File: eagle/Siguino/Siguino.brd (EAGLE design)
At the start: 70.5 x 38.7 mm, 35 parts, among them J1 FTDI Basic, Q1 MOSFET P-CH 20V 5.3A SOT-23, U1 ATMEGA328P_TQFP, U2 LIS3MDLTR_LIS3MDLTR, U3 SPARKFUN-SENSORS_LIS3DH, U4 BME280, Y1 8MHz

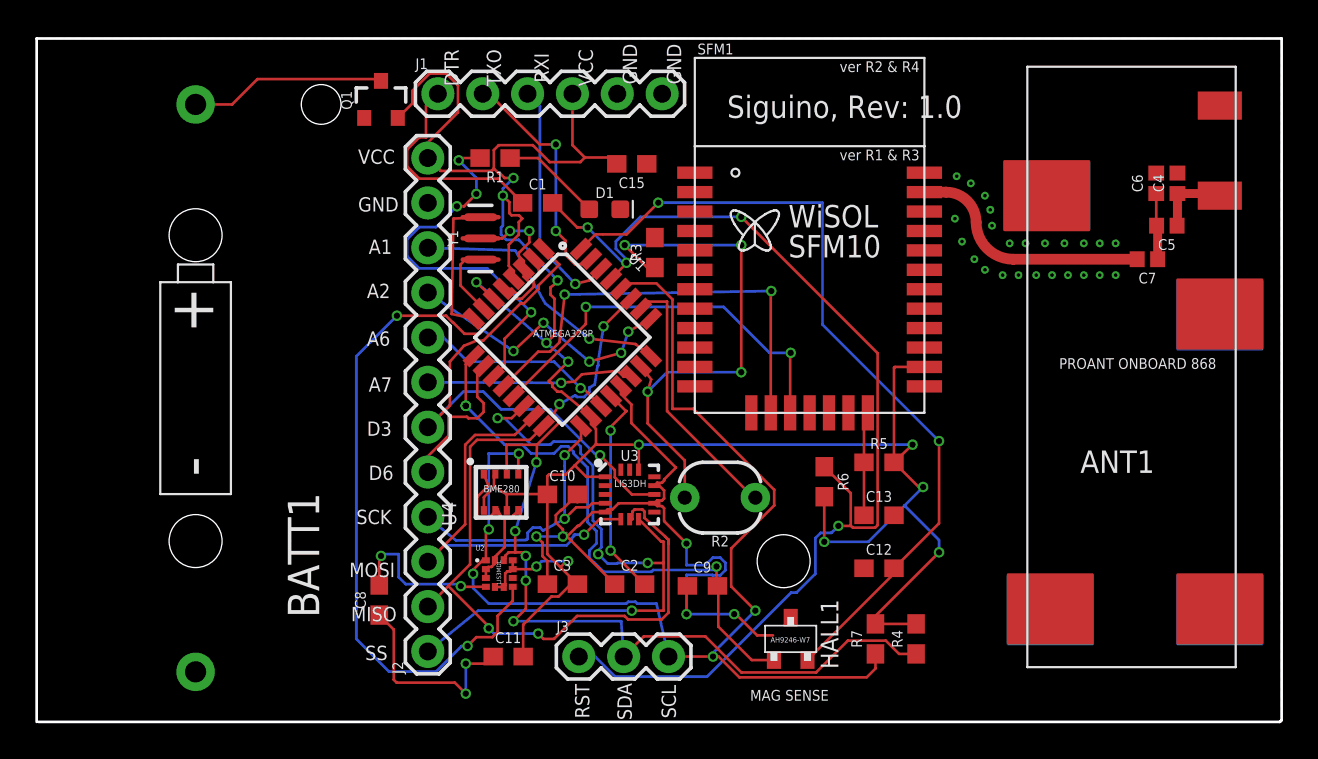
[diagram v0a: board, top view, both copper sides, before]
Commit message: Fixed issue with hatching on antenna pads causing RF issues
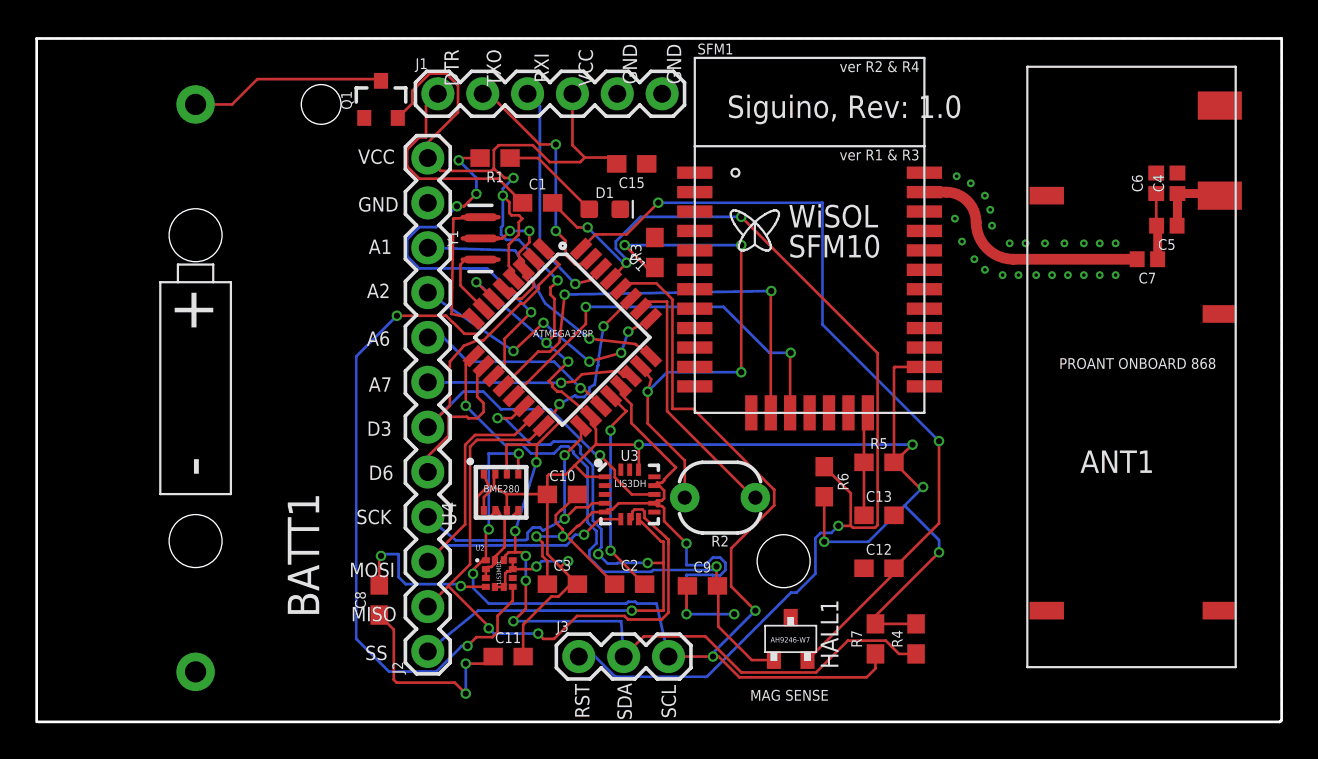
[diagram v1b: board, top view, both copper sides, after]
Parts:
- ANT1: device Siguino:PROANT_ONBOARD_SMD_2400 -> proant:ONBOARD_SMD_2400
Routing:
- net GND: track 76.5 -> 73.0 mm
- net HALL_POWER: vias 3 -> 2
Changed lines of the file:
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@@
 <attribute name="VALUE" x="48.1" y="14.338" size="0.6096" layer="27" font="vector" ratio="20" align="top-center"/>
 </element>
-<element name="ANT1" library="Siguino" package="PROANT_ONBOARD_SMD_2400" value="PROOB471" x="62.4" y="20.5" smashed="yes">
+<element name="ANT1" library="proant" package="ONBOARD_SMD_2400" value="PROOB471" x="62.4" y="20.5" smashed="yes">
 <attribute name="NAME" x="59.5" y="14.5" size="1.27" layer="25"/>
 <attribute name="VALUE" x="59.5" y="18.3" size="1.27" layer="27"/>
@@
 <contactref element="C12" pad="1"/>
 <contactref element="C13" pad="2"/>
-<contactref element="ANT1" pad="GND"/>
 <wire x1="25.54" y1="27.78" x2="26.78" y2="27.78" width="0.1524" layer="1"/>
 <wire x1="26.78" y1="27.78" x2="27.2" y2="28.2" width="0.1524" layer="1"/>
@@
 <wire x1="37.2" y1="6.5" x2="39.9" y2="6.5" width="0.1524" layer="16"/>
 <via x="39.9" y="6.5" extent="1-16" drill="0.35"/>
-<wire x1="39.9" y1="6.5" x2="40" y2="6.5" width="0.1524" layer="1"/>
-<wire x1="40" y1="6.5" x2="41.2" y2="5.3" width="0.1524" layer="1"/>
-<wire x1="41.2" y1="5.3" x2="42.1" y2="5.3" width="0.1524" layer="1"/>
 <contactref element="C15" pad="1"/>
 <contactref element="C6" pad="2"/>
@@
 <wire x1="36.6" y1="14.8" x2="35.9312" y2="14.1312" width="0.1524" layer="1"/>
 <wire x1="35.9312" y1="14.1312" x2="35.9312" y2="14.0566625" width="0.1524" layer="1"/>
-<wire x1="30.3988" y1="11.0988" x2="30.2" y2="10.9" width="0.1524" layer="1"/>
-<wire x1="31.02" y1="12.82880625" x2="31.02" y2="13.28" width="0.1524" layer="1"/>
 <wire x1="35.8133375" y1="12.9388" x2="35.9312" y2="13.0566625" width="0.1524" layer="1"/>
 <wire x1="35.9312" y1="13.0566625" x2="35.9312" y2="13.5033375" width="0.1524" layer="1"/>
@@
 <wire x1="26.35" y1="9.56" x2="26.35" y2="9.3754625" width="0.15" layer="1"/>
 <wire x1="26.35" y1="9.3754625" x2="26.2662" y2="9.2916625" width="0.15" layer="1"/>
+<contactref element="ANT1" pad="GND"/>
 </signal>
 <signal name="VCC">
@@
 <contactref element="U4" pad="P$8"/>
 <contactref element="U4" pad="P$2"/>
-<wire x1="27" y1="12.35" x2="27.025" y2="12.375" width="0.1524" layer="1"/>
 <wire x1="25.725" y1="12.375" x2="25.725" y2="13.125" width="0.1524" layer="1"/>
 <wire x1="25.725" y1="13.125" x2="26.3" y2="13.7" width="0.1524" layer="1"/>
@@
 <wire x1="30.9" y1="25.2" x2="31.70294375" y2="25.4" width="0.1524" layer="1"/>
 <wire x1="31.70294375" y1="25.4" x2="32.356796875" y2="26.053853125" width="0.1524" layer="1"/>
-<wire x1="28.8012" y1="27.3988" x2="28.9" y2="27.3" width="0.1524" layer="16"/>
 <wire x1="28.9" y1="27.3" x2="28.9" y2="35.27" width="0.1524" layer="16"/>
 <wire x1="28.9" y1="35.27" x2="28.2" y2="35.97" width="0.1524" layer="16"/>
@@
 <contactref element="J2" pad="6"/>
 <wire x1="25.31153125" y1="21.98975" x2="25.68975" y2="21.98975" width="0.1524" layer="1"/>
-<wire x1="30" y1="26.3" x2="29.999796875" y2="26.3" width="0.1524" layer="1"/>
 <wire x1="25.31153125" y1="21.98975" x2="24.6" y2="21.7" width="0.1524" layer="1"/>
 <wire x1="24.6" y1="21.7" x2="23.8" y2="20.8" width="0.1524" layer="1"/>
@@
 <wire x1="27.982125" y1="24.08558125" x2="28.820109375" y2="24.923565625" width="0.1524" layer="1"/>
 <wire x1="28.820109375" y1="24.923565625" x2="28.820109375" y2="25.120109375" width="0.1524" layer="1"/>
-<wire x1="28.820109375" y1="25.120109375" x2="30" y2="26.3" width="0.1524" layer="1"/>
+<wire x1="30" y1="26.3" x2="28.820109375" y2="25.120109375" width="0.1524" layer="1"/>
 <contactref element="U3" pad="11"/>
 <wire x1="33.1388" y1="14.2466625" x2="33.1388" y2="14.6612" width="0.1524" layer="1"/>
@@
 <wire x1="24.56" y1="19.1" x2="22.55" y2="17.09" width="0.1524" layer="16"/>
 <contactref element="U1" pad="1"/>
-<wire x1="29.114571875" y1="27.185225" x2="29.114775" y2="27.185225" width="0.15" layer="1"/>
-<wire x1="29.114775" y1="27.185225" x2="30" y2="26.3" width="0.15" layer="1"/>
+<wire x1="29.114571875" y1="27.185225" x2="29.114775" y2="27.185225" width="0.1524" layer="1"/>
+<wire x1="29.114775" y1="27.185225" x2="30" y2="26.3" width="0.1524" layer="1"/>
 </signal>
 <signal name="D6">
@@
 <contactref element="U1" pad="25"/>
 <contactref element="J2" pad="9"/>
-<wire x1="22.56" y1="24.7" x2="22.55" y2="24.71" width="0.1524" layer="16"/>
 <wire x1="22.55" y1="24.71" x2="27.4" y2="21.4" width="0.1524" layer="16"/>
 <via x="27.4" y="21.4" extent="1-16" drill="0.35"/>
@@
 <via x="31.4" y="11" extent="1-16" drill="0.35"/>
 <wire x1="31.4" y1="11" x2="30.9" y2="11" width="0.1524" layer="16"/>
-<wire x1="30.9" y1="11" x2="30.80880625" y2="11" width="0.1524" layer="16"/>
 <wire x1="23.4788" y1="10.3988" x2="22.55" y2="9.47" width="0.1524" layer="16"/>
 <wire x1="30.7012" y1="10.69239375" x2="30.40760625" y2="10.3988" width="0.1524" layer="16"/>
@@
 <signal name="N$4">
 <contactref element="C5" pad="1"/>
-<contactref element="ANT1" pad="RF_FEED"/>
-<wire x1="67.12" y1="29.92" x2="67.4" y2="30.2" width="0.1524" layer="1"/>
-<wire x1="67.22" y1="30.02" x2="67.4" y2="30.2" width="0.1524" layer="1"/>
 <contactref element="C4" pad="1"/>
-<wire x1="66.72" y1="30.32" x2="67.12" y2="29.92" width="0.1524" layer="1"/>
+<wire x1="67.12" y1="29.92" x2="66.72" y2="30.32" width="0.1524" layer="1"/>
 <wire x1="64.98" y1="28.5" x2="65" y2="28.52" width="0.508" layer="1"/>
 <wire x1="65" y1="28.52" x2="65" y2="30.32" width="0.508" layer="1"/>
 <wire x1="65" y1="30.32" x2="66.72" y2="30.32" width="0.508" layer="1"/>
+<contactref element="ANT1" pad="RF_FEED"/>
+<wire x1="67.4" y1="30.2" x2="67.12" y2="29.92" width="0.1524" layer="1"/>
 </signal>
 <signal name="SDA">
@@
 <wire x1="24.7" y1="20.6598" x2="24.7" y2="18.3" width="0.15" layer="1"/>
 <via x="24.7" y="18.3" extent="1-16" drill="0.35"/>
-<via x="24.7" y="18.3" extent="1-16" drill="0.35"/>
 <wire x1="30.0928875" y1="16" x2="30.5071125" y2="16" width="0.15" layer="16"/>
